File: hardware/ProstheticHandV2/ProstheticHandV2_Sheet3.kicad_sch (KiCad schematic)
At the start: 0 parts

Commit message: Started working on PCB
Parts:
- added C12, C14, C15: 100nF, Capacitor_THT:C_Disc_D3.8mm_W2.6mm_P2.50mm, symbol Device:C
- added J4: CONN_SERVO_01, Connector_JST:JST_XA_B03B-XASK-1_1x03_P2.50mm_Vertical, symbol Connector:Conn_01x03_Socket
- added J6: CONN_SERVO_02, Connector_JST:JST_XA_B03B-XASK-1_1x03_P2.50mm_Vertical, symbol Connector:Conn_01x03_Socket
- added J7: CONN_SERVO_03, Connector_JST:JST_XA_B03B-XASK-1_1x03_P2.50mm_Vertical, symbol Connector:Conn_01x03_Socket
- added R19, R24, R27: 0.1, Resistor_THT:R_Axial_DIN0922_L20.0mm_D9.0mm_P30.48mm_Horizontal, symbol Device:R
- added R21, R25, R28: 1k2, Resistor_THT:R_Axial_DIN0207_L6.3mm_D2.5mm_P7.62mm_Horizontal, symbol Device:R
- added R23, R26, R29: 68k, Resistor_THT:R_Axial_DIN0207_L6.3mm_D2.5mm_P7.62mm_Horizontal, symbol Device:R
- added TP20: TP_SERVO_CONTROL_01, TestPoint:TestPoint_Pad_D2.5mm, symbol Connector:TestPoint
- added TP22: TP_SERVO_CURR_RAW_01, TestPoint:TestPoint_Pad_D2.5mm, symbol Connector:TestPoint
- added TP24: TP_SERVO_CONTROL_02, TestPoint:TestPoint_Pad_D2.5mm, symbol Connector:TestPoint
- added TP25: TP_SERVO_CURR_RAW_02, TestPoint:TestPoint_Pad_D2.5mm, symbol Connector:TestPoint
- added TP26: TP_SERVO_CONTROL_03, TestPoint:TestPoint_Pad_D2.5mm, symbol Connector:TestPoint
- added TP27: TP_SERVO_CURR_RAW_03, TestPoint:TestPoint_Pad_D2.5mm, symbol Connector:TestPoint
- added TP28: TP_SERVO_CURR_01, TestPoint:TestPoint_Pad_D2.5mm, symbol Connector:TestPoint
- added TP29: TP_SERVO_CURR_02, TestPoint:TestPoint_Pad_D2.5mm, symbol Connector:TestPoint
- added TP30: TP_SERVO_CURR_03, TestPoint:TestPoint_Pad_D2.5mm, symbol Connector:TestPoint
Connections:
- new net: C14.1, R25.2, R26.1
- new net: J7.1 (Pin_1), R27.1, R28.1, TP27.1
- new net: C15.1, R28.2, R29.1
- new net: J6.1 (Pin_1), R24.1, R25.1, TP25.1
- new net: J4.1 (Pin_1), R19.1, R21.1, TP22.1
- new net: C12.1, R21.2, R23.1
- new net +BATT: J4.2 (Pin_2), J6.2 (Pin_2), J7.2 (Pin_2)
- new net GND: C12.2, C14.2, C15.2, R19.2, R24.2, R27.2
- new net SERVO_CONTROL_01: J4.3 (Pin_3), TP20.1
- new net SERVO_CONTROL_02: J6.3 (Pin_3), TP24.1
- new net SERVO_CONTROL_03: J7.3 (Pin_3), TP26.1
- new net SERVO_CURR_01: R23.2, TP28.1
- new net SERVO_CURR_02: R26.2, TP29.1
- new net SERVO_CURR_03: R29.2, TP30.1
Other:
- note added: "Servo motors"
- note removed: "TODO - 3 servo motors, current sensing for each and MOSFET to control the power/current they get - MOSFETs controlled by op-amps, where uC gives them using PWM signal and sets the max current"

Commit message: Finalize PCB design for china
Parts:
- renumbered C14 to C12, C12 to C13, C15 to C14, J6 to J4, J4 to J5, J7 to J6, R25 to R19, R26 to R20, R23 to R22, R24 to R23, R19 to R24, R28 to R25, R29 to R26, TP24 to TP21, TP20 to TP22, TP25 to TP23, TP29 to TP24, TP22 to TP25, TP28 to TP26, TP26 to TP27, TP27 to TP28, TP30 to TP29

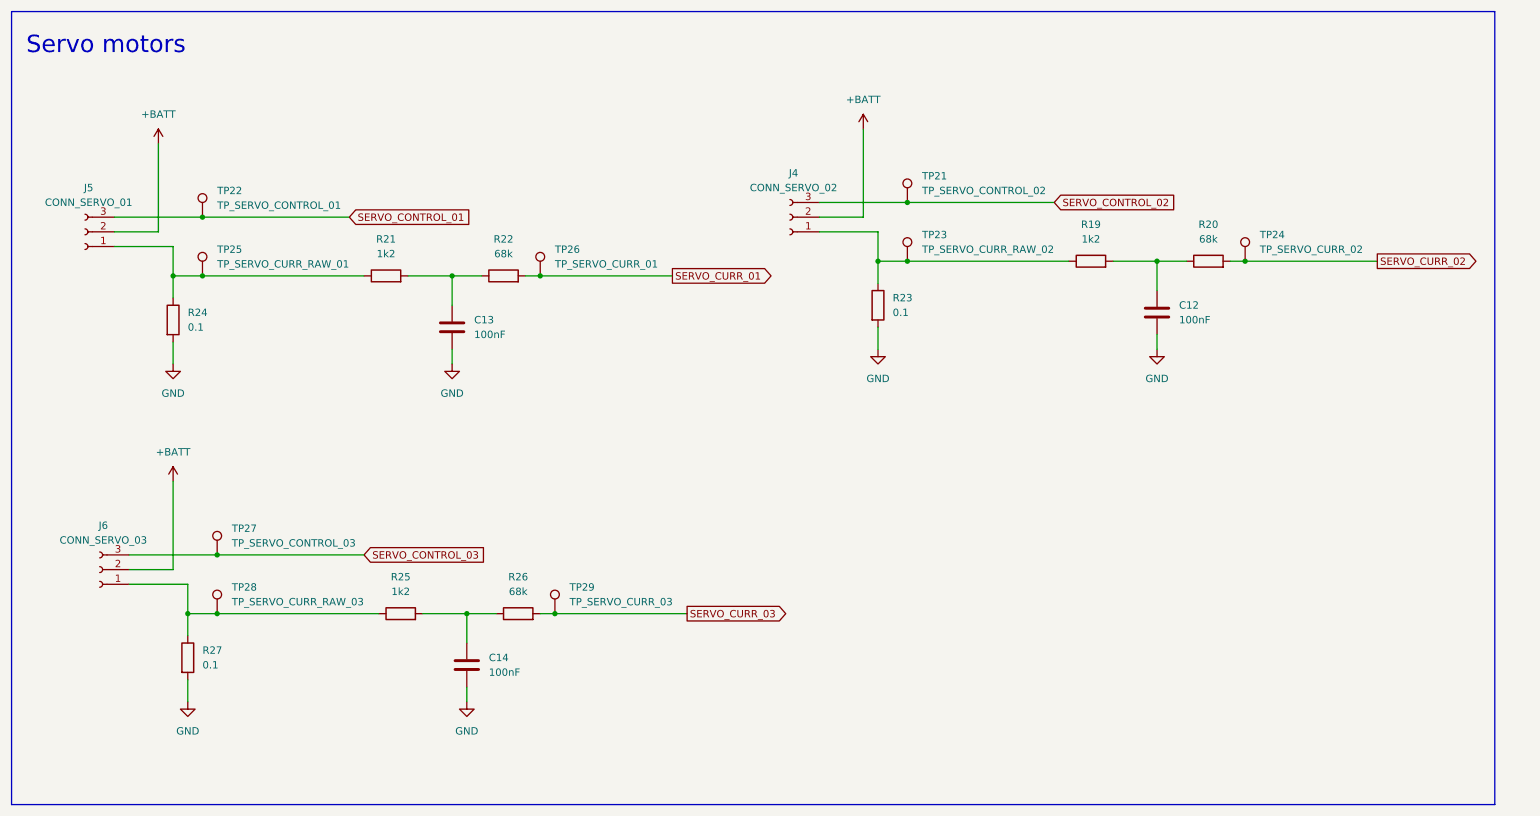
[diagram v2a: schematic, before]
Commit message: Update PCB, sent to JLCPCB
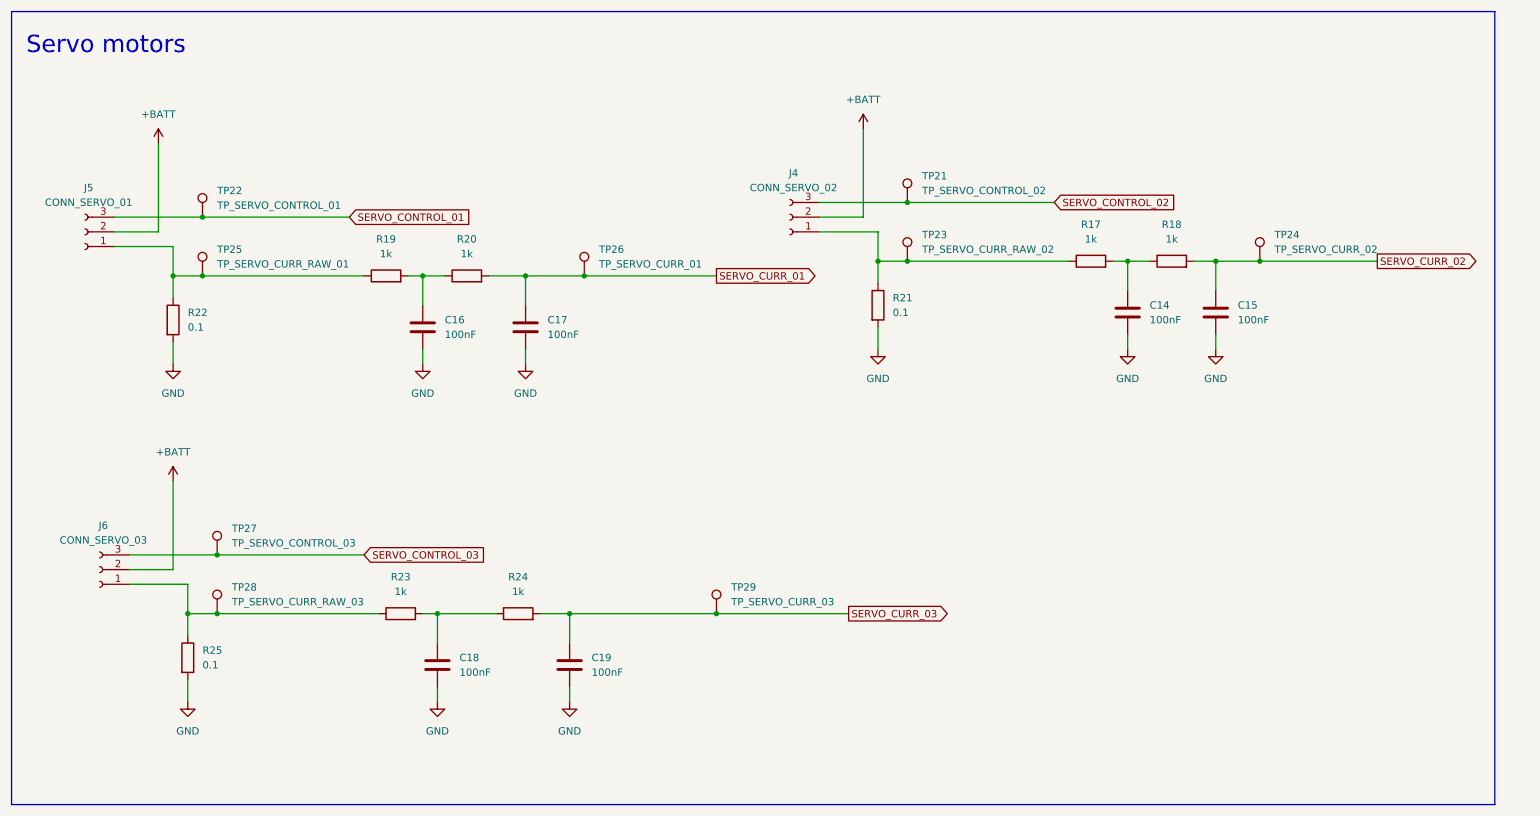
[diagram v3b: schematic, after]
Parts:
- added C15, C17, C19: 100nF, Capacitor_SMD:C_1206_3216Metric, symbol Device:C
- C14: renamed from C12; footprint Capacitor_THT:C_Disc_D3.8mm_W2.6mm_P2.50mm -> Capacitor_SMD:C_1206_3216Metric
- C16: renamed from C13; footprint Capacitor_THT:C_Disc_D3.8mm_W2.6mm_P2.50mm -> Capacitor_SMD:C_1206_3216Metric
- C18: renamed from C14; footprint Capacitor_THT:C_Disc_D3.8mm_W2.6mm_P2.50mm -> Capacitor_SMD:C_1206_3216Metric
- R17: renamed from R19; value 1k2 -> 1k; footprint Resistor_THT:R_Axial_DIN0207_L6.3mm_D2.5mm_P7.62mm_Horizontal -> Resistor_SMD:R_1206_3216Metric
- R18: renamed from R20; value 68k -> 1k; footprint Resistor_THT:R_Axial_DIN0207_L6.3mm_D2.5mm_P7.62mm_Horizontal -> Resistor_SMD:R_1206_3216Metric
- R19: renamed from R21; value 1k2 -> 1k; footprint Resistor_THT:R_Axial_DIN0207_L6.3mm_D2.5mm_P7.62mm_Horizontal -> Resistor_SMD:R_1206_3216Metric
- R20: renamed from R22; value 68k -> 1k; footprint Resistor_THT:R_Axial_DIN0207_L6.3mm_D2.5mm_P7.62mm_Horizontal -> Resistor_SMD:R_1206_3216Metric
- R23: renamed from R25; value 1k2 -> 1k; footprint Resistor_THT:R_Axial_DIN0207_L6.3mm_D2.5mm_P7.62mm_Horizontal -> Resistor_SMD:R_1206_3216Metric
- R24: renamed from R26; value 68k -> 1k; footprint Resistor_THT:R_Axial_DIN0207_L6.3mm_D2.5mm_P7.62mm_Horizontal -> Resistor_SMD:R_1206_3216Metric
- renumbered R23 to R21, R24 to R22, R27 to R25
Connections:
- net GND: now also C15.2, C17.2, C19.2
- net SERVO_CURR_01: now also C17.1
- net SERVO_CURR_02: now also C15.1
- net SERVO_CURR_03: now also C19.1
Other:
- moved on the sheet: C14, C16, C18, R18, R20, TP24, TP26, TP29
